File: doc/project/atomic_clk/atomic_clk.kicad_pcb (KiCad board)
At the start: 2 copper layers, 47.8 x 30.2 mm, 23 parts, among them J1 Goldpin, J2 Cell+, J3 Cell-, SW1 POWER, SW2 SET, SW3 CLEAR, U1 BQ-M322RD, U2 STM32F030F4Px, U3 TC1185-3.3VCT8, Y1 18.432MHz

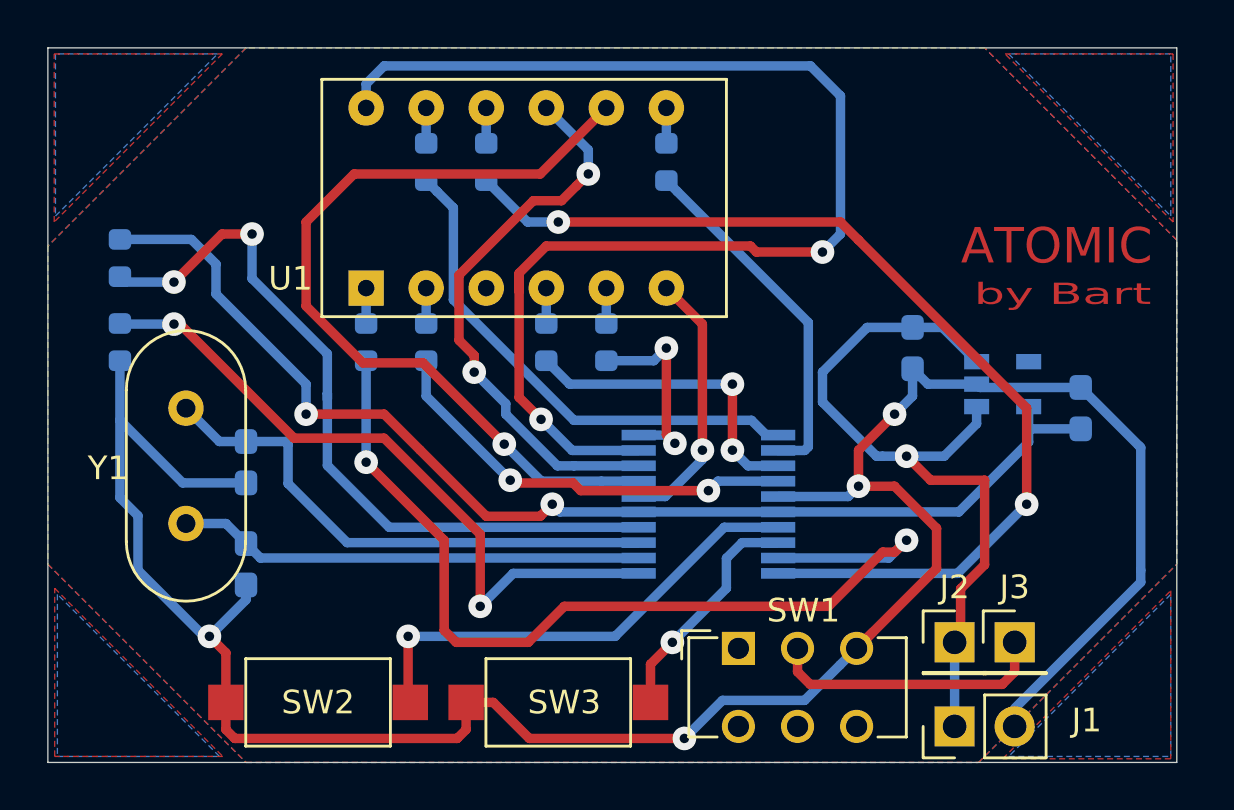
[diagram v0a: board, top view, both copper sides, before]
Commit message: przygotowanie pod nowy akumulator
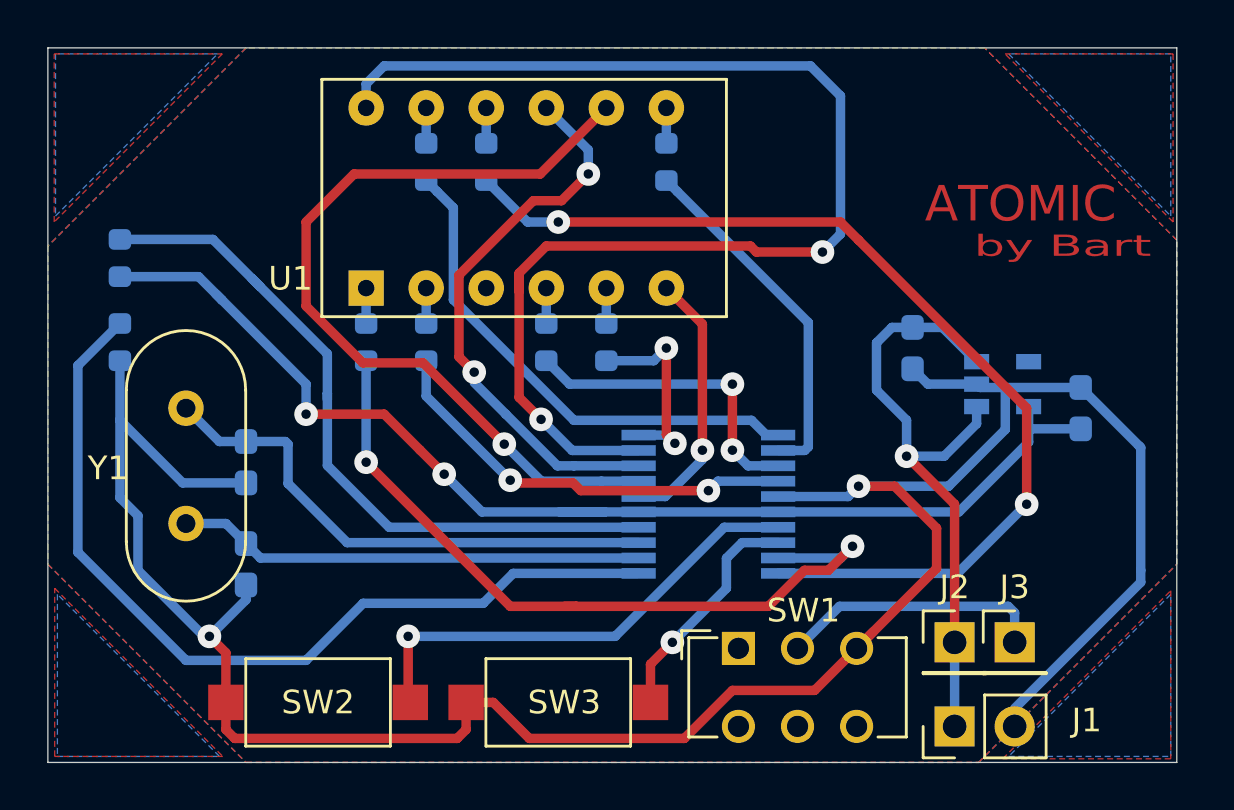
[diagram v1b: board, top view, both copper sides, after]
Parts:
- turned R9 to 90 degrees
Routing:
- net Net-(R8-Pad1): track 29.3 -> 37.6 mm, vias 2 -> 0
- net SE: track 40.4 -> 32.6 mm
- net Net-(C3-Pad1): track 32.6 -> 27.3 mm
- net GND: track 102.5 -> 105.5 mm, vias 4 -> 2
- net Net-(R9-Pad2): track 32.1 -> 30.5 mm, vias 2 -> 0
- net +3V3: track 50.1 -> 50.8 mm
- net Net-(J3-Pad1): track 11.9 -> 11.3 mm

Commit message: jst conetor
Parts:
- removed J3: Cell-, Connector_PinHeader_2.54mm:PinHeader_1x01_P2.54mm_Vertical
- J2: value Cell+ -> Bat; footprint Connector_PinHeader_2.54mm:PinHeader_1x01_P2.54mm_Vertical -> Connector_PinHeader_1.27mm:PinHeader_1x02_P1.27mm_Vertical
- moved J2 9.92 mm to (246.6, 110.2), turned to 180 degrees
- moved C4 5.29 mm to (241.3, 102.4), turned to 180 degrees
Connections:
- J2 pad 1: Net-(C3-Pad1) -> Net-(J2-Pad1)
- SW1 pad 2: Net-(J3-Pad1) -> Net-(J2-Pad1)
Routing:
- net Net-(J2-Pad1): track 0.00 -> 17.5 mm
- net Net-(C3-Pad1): track 27.3 -> 44.8 mm, vias 1 -> 2
- net Net-(J3-Pad1): track 11.3 -> 0.00 mm
- net GND: track 105.5 -> 97.9 mm
- net +3V3: track 50.8 -> 54.3 mm
